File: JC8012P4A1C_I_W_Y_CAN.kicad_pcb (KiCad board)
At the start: 2 copper layers, 66 x 54 mm, 31 parts, among them J1 61201022921, J2 68711414522, J3 653104131822, Q1 DMP6050SSD, U1 TLE9250VSJ, U2 171030601

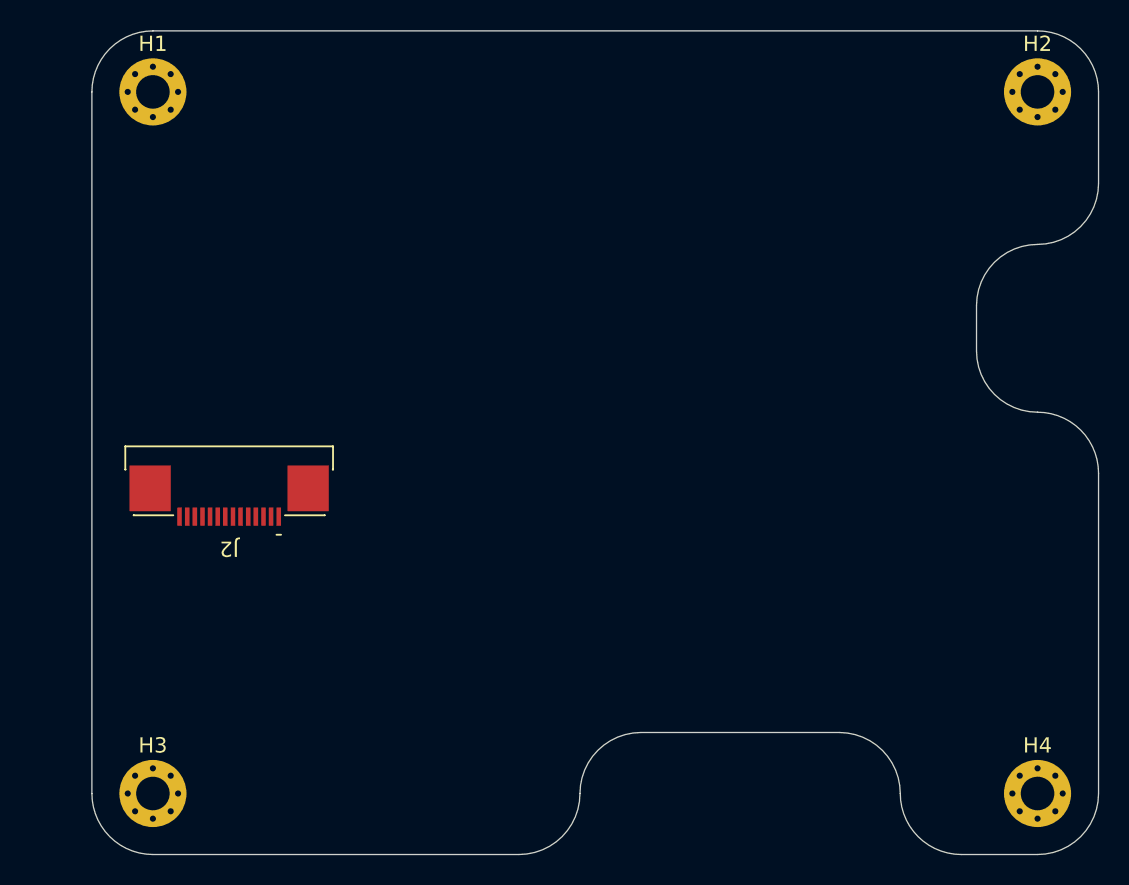
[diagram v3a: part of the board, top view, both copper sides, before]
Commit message: Third notch for CN5, R2 notch corners, move J2
- New notch on the left edge for the 3x2 pin header CN5 of the display
  board (y 127-139, 4.5 mm deep)
- Electrolytic notch moved down (y 116.5-127.5), CR1220 notch 8.5 mm deep
  (x 132.5-153); positions checked with a 1:1 paper template
- All notch corners R2, outer corners R4 centred on the mounting holes
- J2 moved 4 mm right (x 113) to clear the CN5 notch

Co-Authored-By: Claude Opus 5.5 <noreply@anthropic.com>
Claude-Session: https://claude.ai/code/session_014h8cGi8SRWthYdGFH1Qgzz
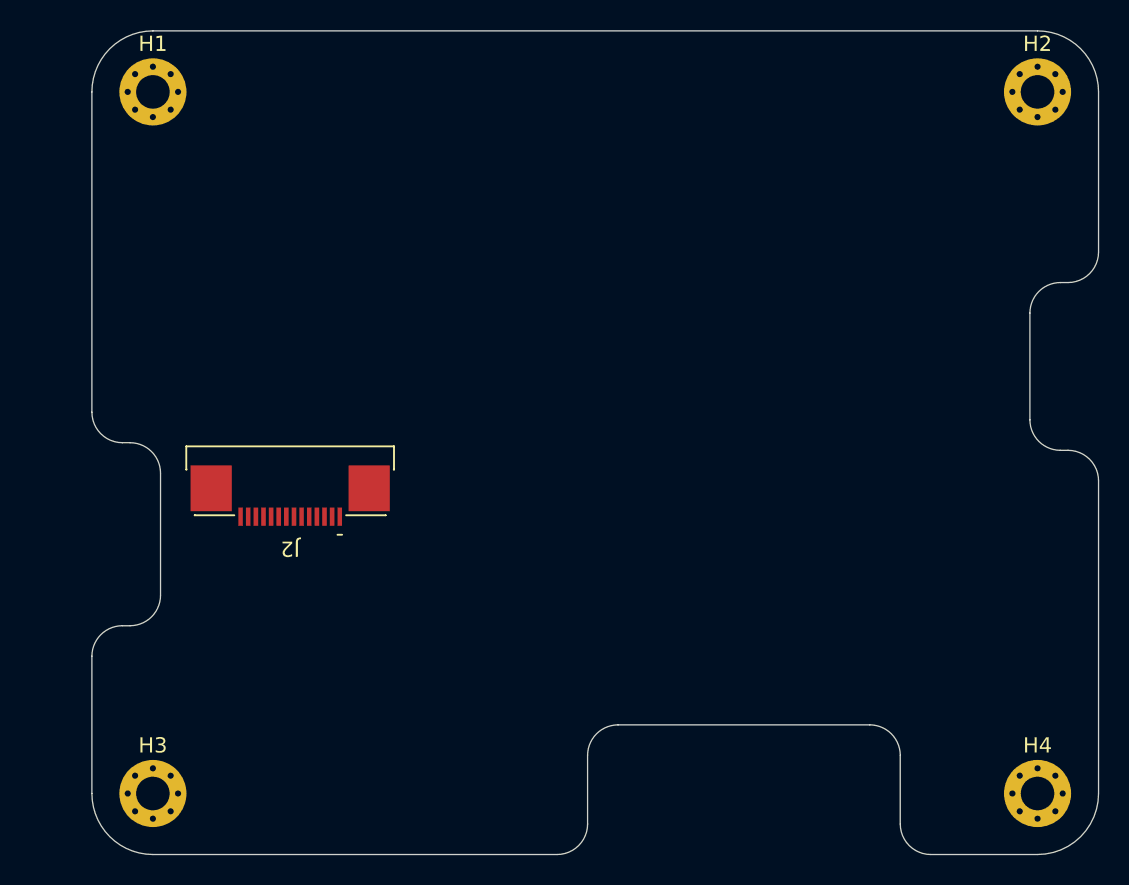
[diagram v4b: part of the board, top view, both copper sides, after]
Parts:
- moved J2 4.00 mm to (113.0, 129.5)
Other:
- outline, holes or cut-outs redrawn
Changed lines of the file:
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@@
 	(footprint "JC8012P4A1C_CAN:J_Wurth_WR-FPC_68711414522"
 		(layer "F.Cu")
-		(at 109 129.5 180)
+		(at 113 129.5 180)
 		(descr "Zero Insertion Force Connectors - 0.50mm, body 13.4x4.3x2.1mm, https://www.we-online.com/en/components/products/datasheet/68711414522?ki")
 		(tags "SMT Horizontal")
@@
 	)
 	(gr_line
-		(start 100 150)
+		(start 100 125)
 		(end 100 104)
 		(stroke
@@
 		(layer "Edge.Cuts")
 	)
+	(gr_arc
+		(start 100 141)
+		(mid 100.585786 139.585786)
+		(end 102 139)
+		(stroke
+			(width 0.05)
+			(type default)
+		)
+		(layer "Edge.Cuts")
+	)
+	(gr_line
+		(start 100 150)
+		(end 100 141)
+		(stroke
+			(width 0.05)
+			(type default)
+		)
+		(layer "Edge.Cuts")
+	)
+	(gr_arc
+		(start 102 127)
+		(mid 100.585786 126.414213)
+		(end 100 125)
+		(stroke
+			(width 0.05)
+			(type default)
+		)
+		(layer "Edge.Cuts")
+	)
+	(gr_line
+		(start 102 139)
+		(end 102.5 139)
+		(stroke
+			(width 0.05)
+			(type default)
+		)
+		(layer "Edge.Cuts")
+	)
+	(gr_line
+		(start 102.5 127)
+		(end 102 127)
+		(stroke
+			(width 0.05)
+			(type default)
+		)
+		(layer "Edge.Cuts")
+	)
+	(gr_arc
+		(start 102.5 127)
+		(mid 103.914214 127.585786)
+		(end 104.5 129)
+		(stroke
+			(width 0.05)
+			(type default)
+		)
+		(layer "Edge.Cuts")
+	)
 	(gr_line
 		(start 104 100)
@@
 		(layer "Edge.Cuts")
 	)
+	(gr_arc
+		(start 104.5 137)
+		(mid 103.914214 138.414214)
+		(end 102.5 139)
+		(stroke
+			(width 0.05)
+			(type default)
+		)
+		(layer "Edge.Cuts")
+	)
 	(gr_line
-		(start 128 154)
+		(start 104.5 137)
+		(end 104.5 129)
+		(stroke
+			(width 0.05)
+			(type default)
+		)
+		(layer "Edge.Cuts")
+	)
+	(gr_line
+		(start 130.5 154)
 		(end 104 154)
 		(stroke
@@
 		(layer "Edge.Cuts")
 	)
+	(gr_line
+		(start 132.5 147.5)
+		(end 132.5 152)
+		(stroke
+			(width 0.05)
+			(type default)
+		)
+		(layer "Edge.Cuts")
+	)
 	(gr_arc
-		(start 132 150)
-		(mid 130.828427 152.828427)
-		(end 128 154)
+		(start 132.5 147.5)
+		(mid 133.085786 146.085786)
+		(end 134.5 145.5)
 		(stroke
 			(width 0.05)
@@
 	)
 	(gr_arc
-		(start 132 150)
-		(mid 133.171573 147.171573)
-		(end 136 146)
+		(start 132.5 152)
+		(mid 131.914213 153.414213)
+		(end 130.5 154)
 		(stroke
 			(width 0.05)
@@
 	)
 	(gr_line
-		(start 149 146)
-		(end 136 146)
+		(start 151 145.5)
+		(end 134.5 145.5)
 		(stroke
 			(width 0.05)
@@
 	)
 	(gr_arc
-		(start 149 146)
-		(mid 151.828427 147.171573)
-		(end 153 150)
+		(start 151 145.5)
+		(mid 152.414214 146.085786)
+		(end 153 147.5)
+		(stroke
+			(width 0.05)
+			(type default)
+		)
+		(layer "Edge.Cuts")
+	)
+	(gr_line
+		(start 153 152)
+		(end 153 147.5)
 		(stroke
 			(width 0.05)
@@
 	)
 	(gr_arc
-		(start 157 154)
-		(mid 154.171572 152.828427)
-		(end 153 150)
+		(start 155 154)
+		(mid 153.585786 153.414213)
+		(end 153 152)
 		(stroke
 			(width 0.05)
@@
 	)
 	(gr_line
-		(start 158 118)
-		(end 158 121)
+		(start 161.5 118.5)
+		(end 161.5 125.5)
 		(stroke
 			(width 0.05)
@@
 	)
 	(gr_arc
-		(start 158 118)
-		(mid 159.171573 115.171573)
-		(end 162 114)
+		(start 161.5 118.5)
+		(mid 162.085786 117.085786)
+		(end 163.5 116.5)
 		(stroke
 			(width 0.05)
@@
 		(layer "Edge.Cuts")
 	)
-	(gr_arc
-		(start 162 125)
-		(mid 159.171573 123.828427)
-		(end 158 121)
+	(gr_line
+		(start 162 154)
+		(end 155 154)
 		(stroke
 			(width 0.05)
@@
 	)
 	(gr_arc
-		(start 162 125)
-		(mid 164.828427 126.171572)
-		(end 166 129)
+		(start 163.5 127.5)
+		(mid 162.085786 126.914214)
+		(end 161.5 125.5)
 		(stroke
 			(width 0.05)
@@
 	)
 	(gr_line
-		(start 162 154)
-		(end 157 154)
+		(start 163.5 127.5)
+		(end 164 127.5)
+		(stroke
+			(width 0.05)
+			(type default)
+		)
+		(layer "Edge.Cuts")
+	)
+	(gr_line
+		(start 164 116.5)
+		(end 163.5 116.5)
+		(stroke
+			(width 0.05)
+			(type default)
+		)
+		(layer "Edge.Cuts")
+	)
+	(gr_arc
+		(start 164 127.5)
+		(mid 165.414213 128.085786)
+		(end 166 129.5)
 		(stroke
 			(width 0.05)
@@
 	(gr_line
 		(start 166 104)
-		(end 166 110)
+		(end 166 114.5)
 		(stroke
 			(width 0.05)
@@
 	)
 	(gr_arc
-		(start 166 110)
-		(mid 164.828427 112.828427)
-		(end 162 114)
+		(start 166 114.5)
+		(mid 165.414213 115.914213)
+		(end 164 116.5)
 		(stroke
 			(width 0.05)
@@
 	)
 	(gr_line
-		(start 166 129)
+		(start 166 129.5)
 		(end 166 150)
 		(stroke

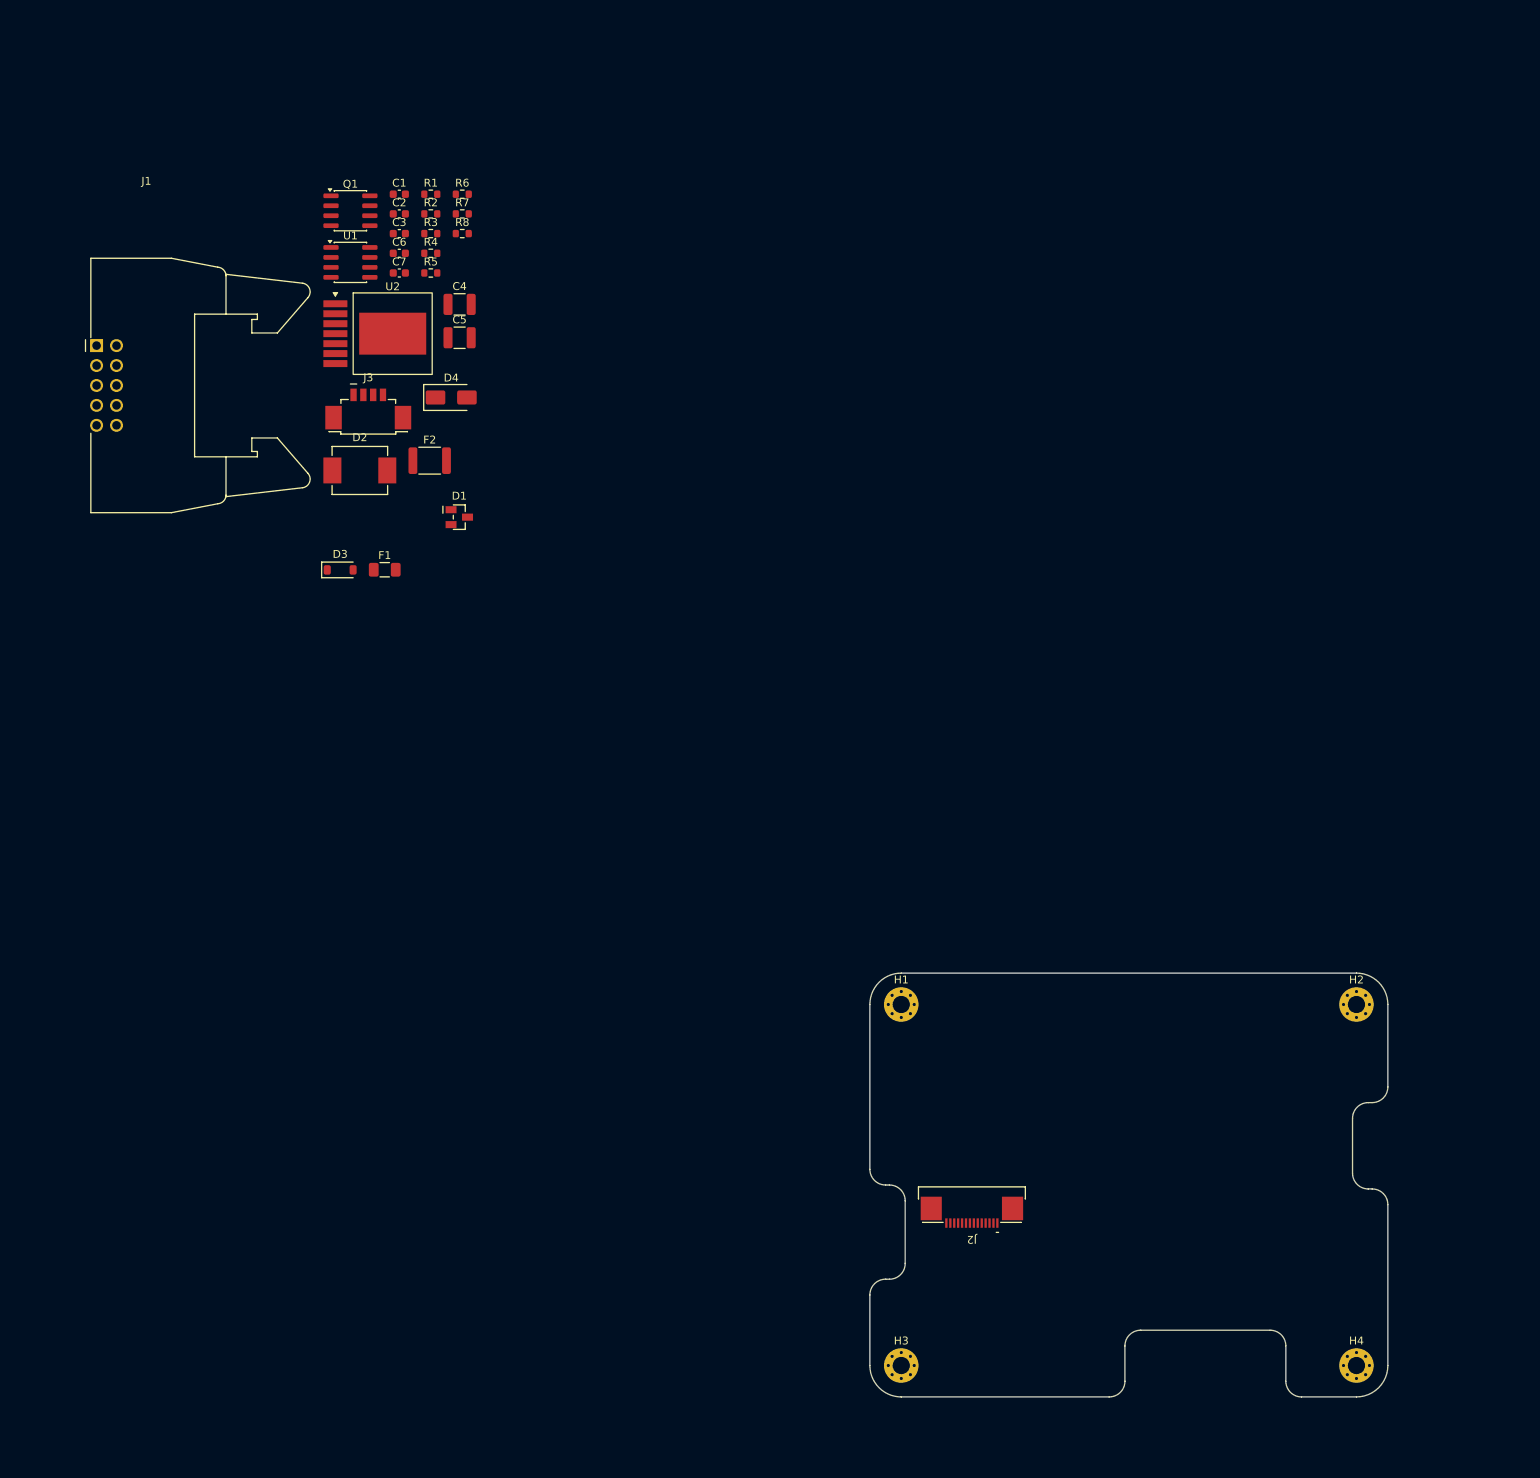
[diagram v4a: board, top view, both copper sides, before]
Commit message: J1: SMT right-angled pin header instead of THT box header
- J1 is now Wuerth WR-PHD 610110249121 (2x5, 2.54 mm, SMT, right
  angled, 6.5 mm high). The former WR-BHD 61201022921 was a THT angled
  box header with long levers (32 x 28 mm) and too big; a straight SMT
  box header would be too high (only ~8 mm free under the cover).
  The board is now SMT only, all parts on the top side.
- Same pinout, J1 rewired in the schematic (netlist checked)
- J1 placed at the bottom edge left of the CR1220 notch, pins towards
  the edge (ribbon cable leaves downwards)
- Polarisation without shroud: cut pin 10 and close position 10 of the
  IDC socket with a coding plug (pins 9/10 unused), see README
- README: mechanics section (stack height, holes, notches)
- Old part removed from the project library

Co-Authored-By: Claude Opus 5.5 <noreply@anthropic.com>
Claude-Session: https://claude.ai/code/session_014h8cGi8SRWthYdGFH1Qgzz
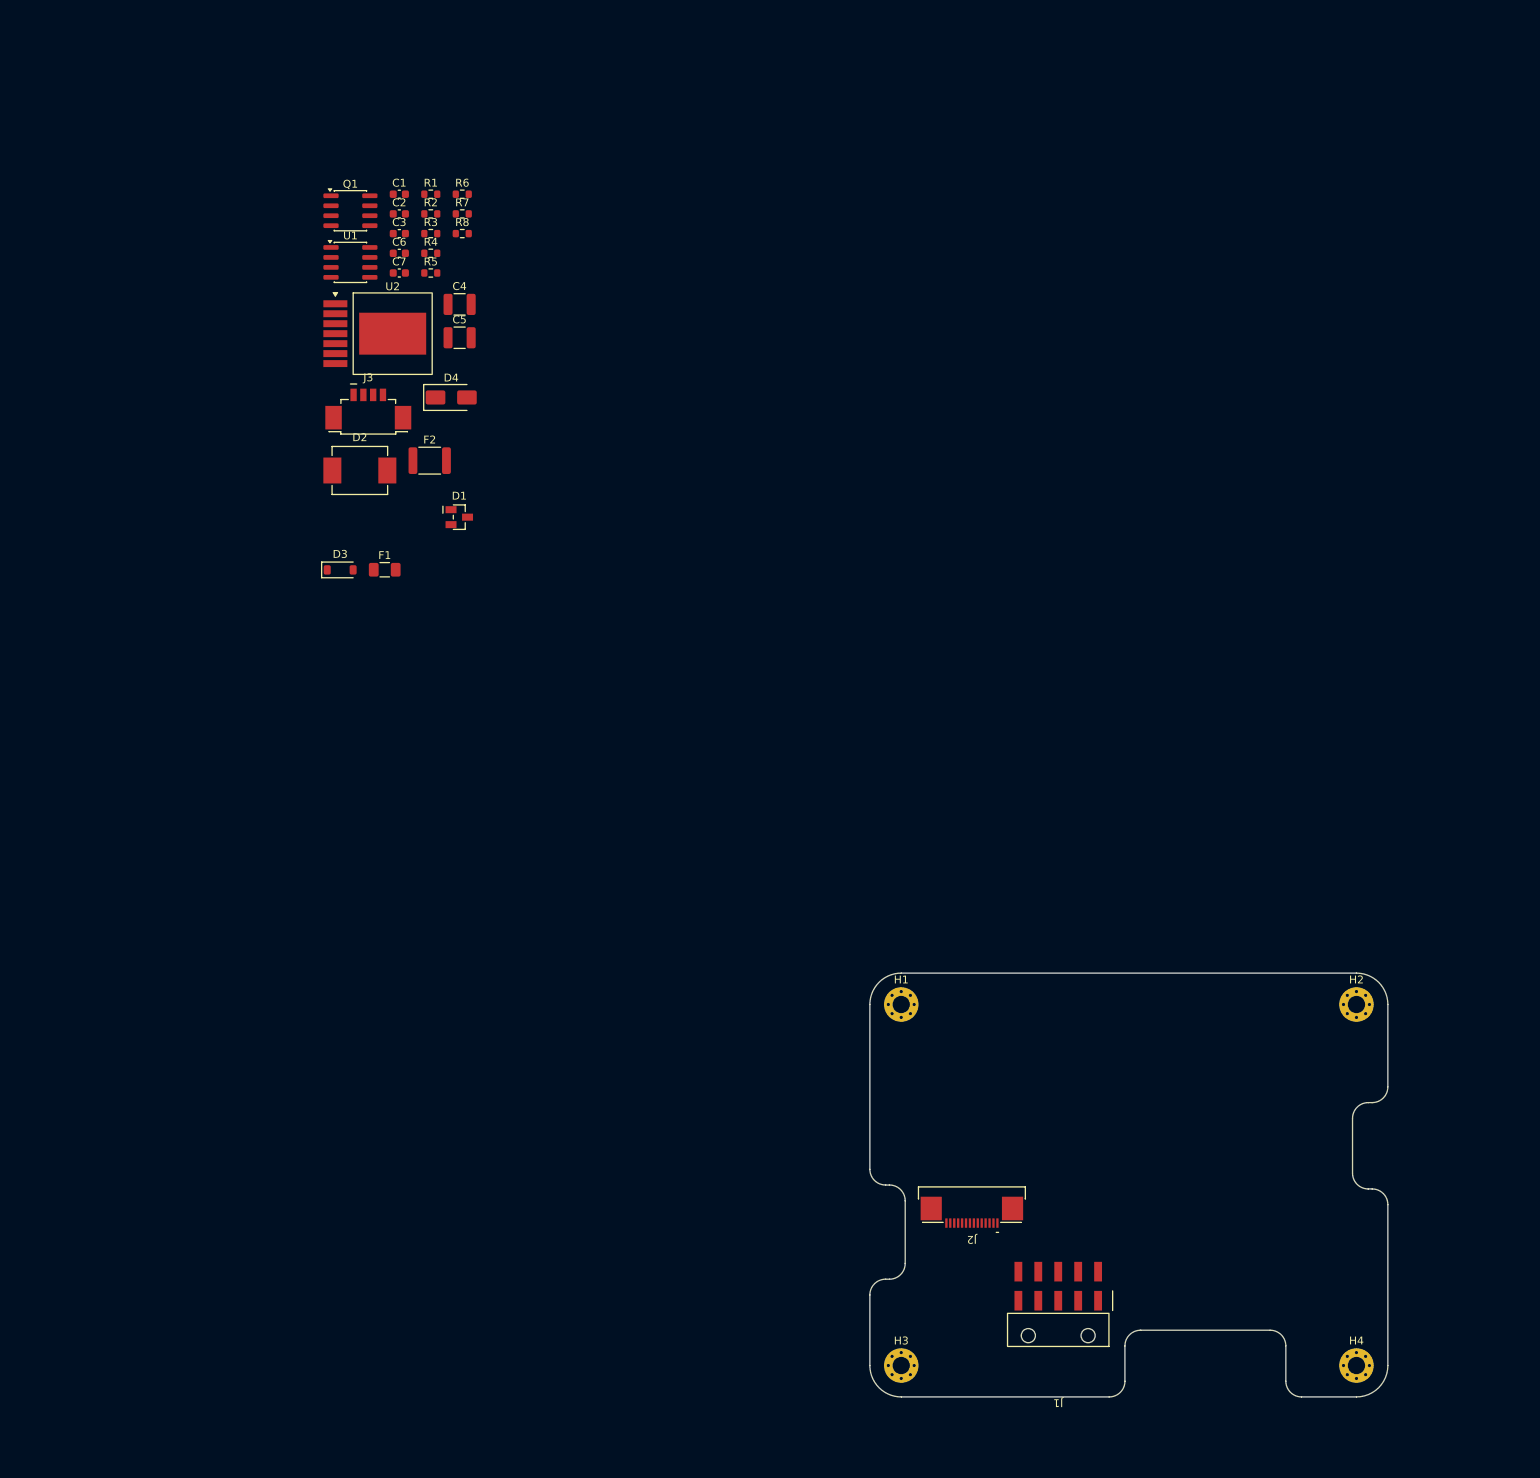
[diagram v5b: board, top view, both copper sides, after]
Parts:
- J1: value 61201022921 -> 610110249121; footprint JC8012P4A1C_CAN:J_Wurth_WR-BHD_61201022921 -> JC8012P4A1C_CAN:J_Wurth_WR-PHD_610110249121
- moved J1 175.3 mm to (124.0, 145.5), turned to 180 degrees

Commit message: J3 mounting tabs to GND, J1 flush with the board edge
- J3 (WR-WTB 653104131822) symbol: added pins MP1/MP2 for the solder
  tabs of the footprint, connected to GND. Removes the two F8 warnings
  "no net for J3 pad MP1/MP2".
- J1 moved so that the plastic body is flush with the bottom board
  edge; only the pins stick out, so the IDC socket can be plugged in.
  The two 1.8 mm locating holes are 0.37 mm from the routed edge
  (JLCPCB states no NPTH-to-edge rule; a broken web is harmless).

Co-Authored-By: Claude Opus 5.5 <noreply@anthropic.com>
Claude-Session: https://claude.ai/code/session_014h8cGi8SRWthYdGFH1Qgzz
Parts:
- moved J1 6.54 mm to (124.0, 152.0)
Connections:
- J3 pad MP1: (no net) -> /GND
- J3 pad MP2: (no net) -> /GND
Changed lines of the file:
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@@
 	(footprint "JC8012P4A1C_CAN:J_Wurth_WR-PHD_610110249121"
 		(layer "F.Cu")
-		(at 124 145.46 180)
+		(at 124 152 180)
 		(descr "2.54 mm SMT Pin Header Double Row Right Angled, body 12.7x16.16x6.48mm, https://www.we-online.com/en/components/products/datasheet/610110249121?ki")
 		(tags "SMT")
@@
 			(unit
 				(name "A")
-				(pins "1" "2" "3" "4")
+				(pins "MP1" "1" "2" "3" "4" "MP2")
 			)
 		)
@@
 			(size 2.1 3)
 			(layers "F.Cu" "F.Mask" "F.Paste")
+			(net "/GND")
+			(pinfunction "MP_MP1")
+			(pintype "passive")
 			(thermal_bridge_angle 45)
 		)
@@
 			(size 2.1 3)
 			(layers "F.Cu" "F.Mask" "F.Paste")
+			(net "/GND")
+			(pinfunction "MP_MP2")
+			(pintype "passive")
 			(thermal_bridge_angle 45)
 		)
